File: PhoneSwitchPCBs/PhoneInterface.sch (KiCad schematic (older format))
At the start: 14 parts

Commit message: Update notes based on changing plans, minor changes to schematics and sim files
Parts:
- removed K?: Relay_DPDT, symbol PhoneInterfaceParts:Relay_DPDT
- added K?: EC2-5NU, Relay_THT:Relay_DPDT_Kemet_EC2, symbol Relay:EC2-5NU
- C? (x2): value 3.9u -> 3.3u
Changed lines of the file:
@@
 P 5250 2850
 F 0 "C?" H 5158 2804 50  0000 R CNN
-F 1 "3.9u" H 5158 2895 50  0000 R CNN
+F 1 "3.3u" H 5158 2895 50  0000 R CNN
 F 2 "" H 5250 2850 50  0001 C CNN
 F 3 "~" H 5250 2850 50  0001 C CNN
@@
 P 5250 4350
 F 0 "C?" H 5158 4304 50  0000 R CNN
-F 1 "3.9u" H 5158 4395 50  0000 R CNN
+F 1 "3.3u" H 5158 4395 50  0000 R CNN
 F 2 "" H 5250 4350 50  0001 C CNN
 F 3 "~" H 5250 4350 50  0001 C CNN
@@
 Wire Wire Line
 	5700 3650 5700 3800
-$Comp
-L PhoneInterfaceParts:Relay_DPDT K?
-U 1 1 60F6CD2F
-P 4400 3800
-F 0 "K?" V 5167 3800 50  0000 C CNN
-F 1 "Relay_DPDT" V 5076 3800 50  0000 C CNN
-F 2 "" H 4400 3800 50  0001 C CNN
-F 3 "" H 4400 3800 50  0001 C CNN
-	1    4400 3800
-	0    -1   -1   0
-$EndComp
 Wire Wire Line
 	5700 3650 4900 3650
@@
 Text Label 5450 3650 0    50   ~ 0
 RING
+$Comp
+L Relay:EC2-5NU K?
+U 1 1 60F657D7
+P 4400 3800
+F 0 "K?" V 5167 3800 50  0000 C CNN
+F 1 "EC2-5NU" V 5076 3800 50  0000 C CNN
+F 2 "Relay_THT:Relay_DPDT_Kemet_EC2" H 4400 3800 50  0001 C CNN
+F 3 "https://content.kemet.com/datasheets/KEM_R7002_EC2_EE2.pdf" H 4400 3800 50  0001 C CNN
+	1    4400 3800
+	0    -1   -1   0
+$EndComp
 $EndSCHEMATC

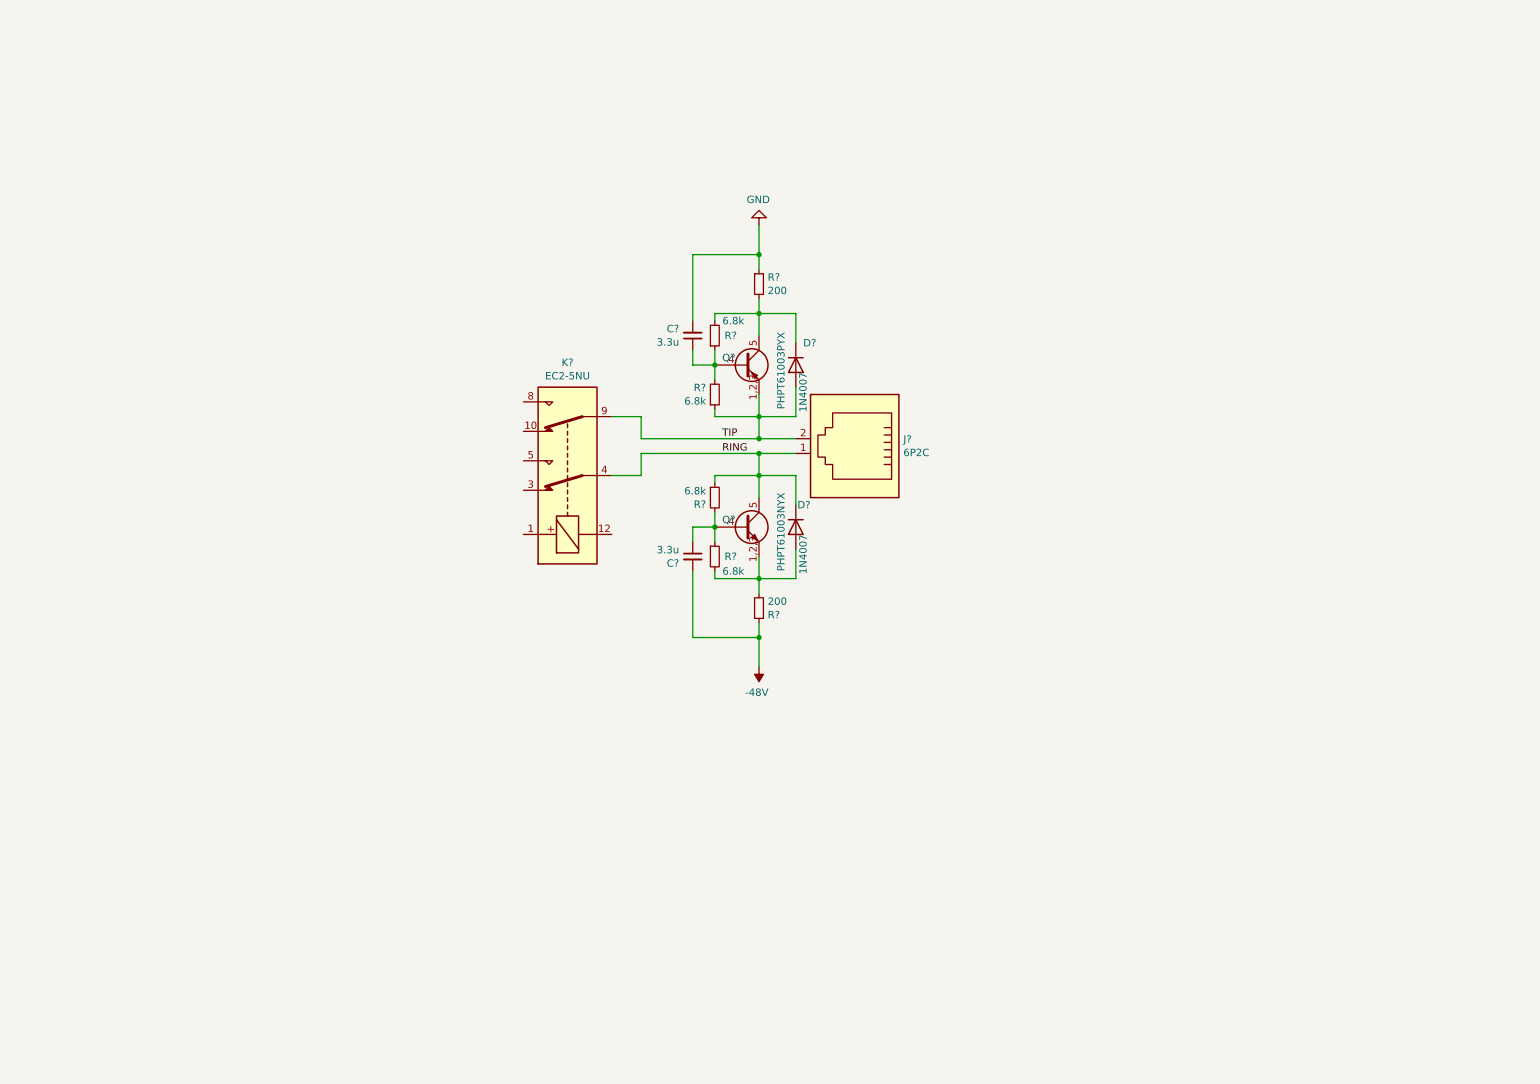
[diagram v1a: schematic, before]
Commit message: Updated schematics and notes
Changed pin count for using analog switch bypass of ring cut filter, worked more on schematics, including deciding to put routing on line modules.
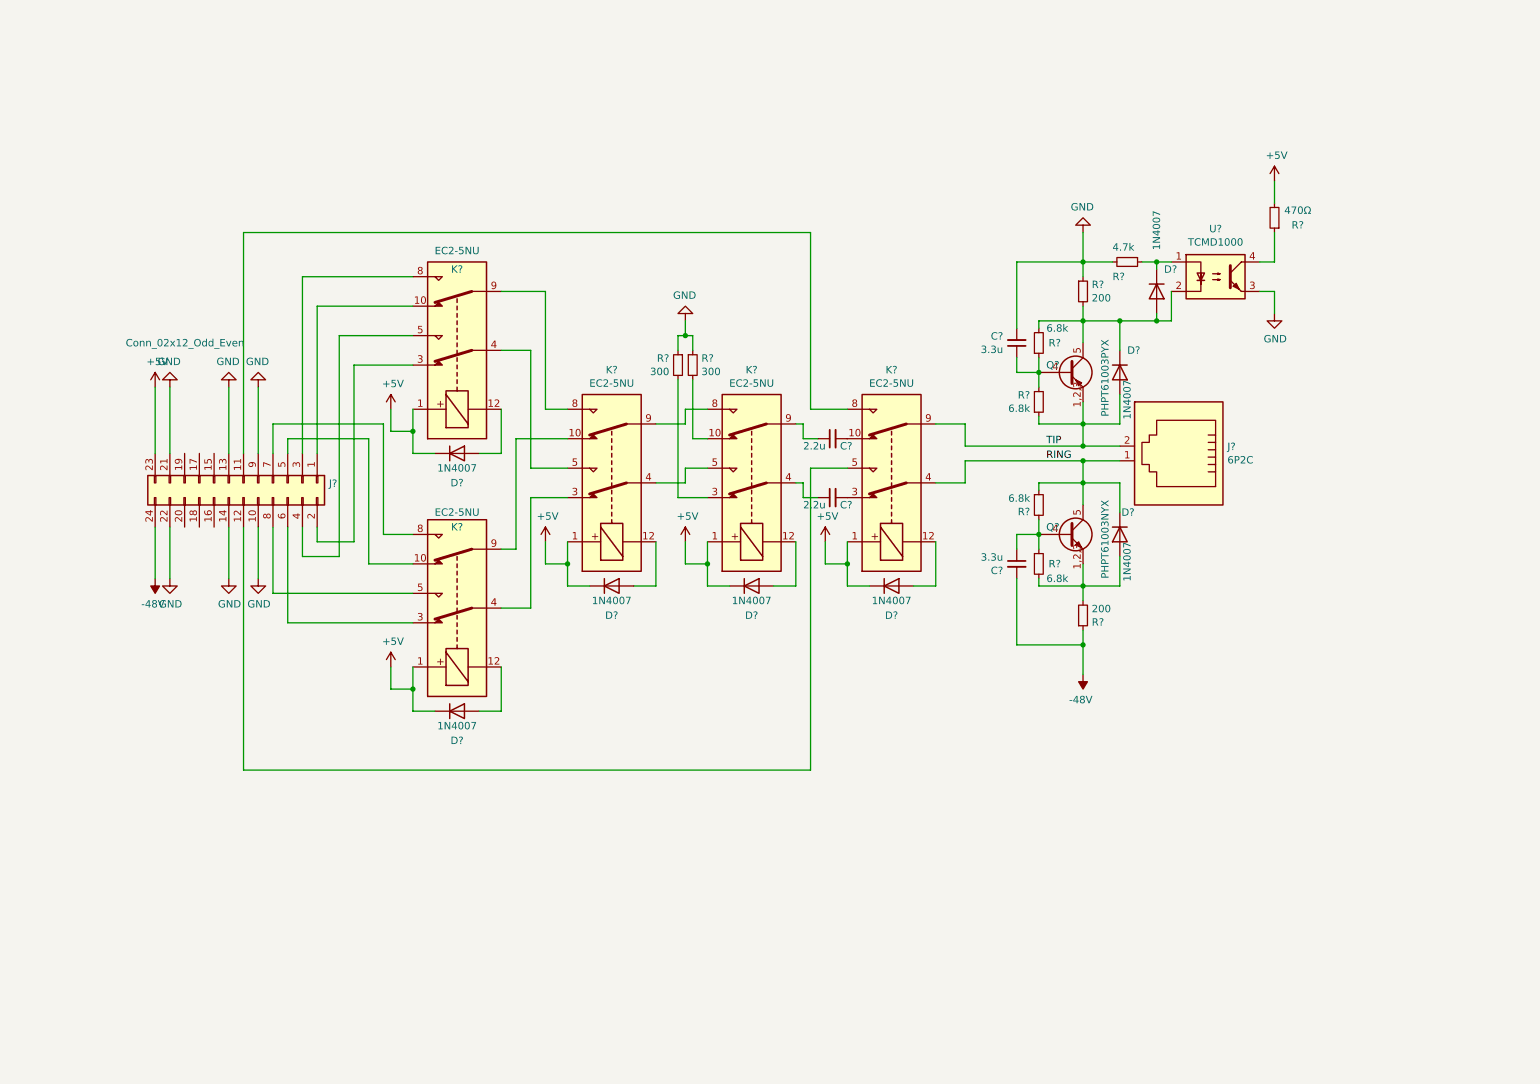
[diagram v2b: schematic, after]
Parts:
- added C? (x2): 2.2u, symbol Device:C_Small
- added D? (x6): 1N4007, Diode_THT:D_DO-41_SOD81_P10.16mm_Horizontal, symbol Diode:1N4007
- added J?: Conn_02x12_Odd_Even, symbol Connector_Generic:Conn_02x12_Odd_Even
- added K? (x4): EC2-5NU, Relay_THT:Relay_DPDT_Kemet_EC2, symbol Relay:EC2-5NU
- added R?: 4.7k, symbol Device:R_Small
- added R?: 470Ω, symbol Device:R_Small
- added R? (x2): 300, symbol Device:R_Small
- added U?: TCMD1000, Package_SO:SOP-4_4.4x2.6mm_P1.27mm, symbol PhoneInterfaceParts:TCMD1000
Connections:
- net -48V: now also J?.24 (Pin_24)
- net GND: now also J?.10 (Pin_10), J?.13 (Pin_13), J?.14 (Pin_14), J?.21 (Pin_21), J?.22 (Pin_22), J?.9 (Pin_9), R?.1, R?.1, R?.2, U?.3
- net at D?.1 (K), Q?.5 (C), R?.2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: now also D?.2 (A), U?.2
- net +5V: now reaches K?.1
- net +5V: now also D?.1 (K), D?.1 (K), D?.1 (K), D?.1 (K), D?.1 (K), J?.23 (Pin_23), K?.1, K?.1, K?.1, K?.1, R?.2
- net at K?.10: now also C?.2
- net at K?.12: now also D?.2 (A)
- net at K?.3: now also C?.2
- net at K?.5: now also J?.12 (Pin_12)
- net at K?.8: now also J?.11 (Pin_11)
- new net: D?.1 (K), R?.1, U?.1
- new net: R?.1, U?.4
- new net: K?.10, R?.2
- new net: D?.2 (A), K?.12 (x4)
- new net: K?.3, R?.2
- new net: C?.1, K?.4
- new net: K?.4, K?.5 (x2)
- new net: K?.8, K?.9 (x2)
- new net: C?.1, K?.9
- new net: K?.10, K?.9
- new net: K?.3, K?.4
- new net: J?.1 (Pin_1), K?.10
- new net: J?.2 (Pin_2), K?.3
- new net: J?.4 (Pin_4), K?.5
- new net: J?.3 (Pin_3), K?.8
- new net: J?.5 (Pin_5), K?.10
- new net: J?.6 (Pin_6), K?.3
- new net: J?.8 (Pin_8), K?.5
- new net: J?.7 (Pin_7), K?.8
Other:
- moved on the sheet: C?, D?, J?, K?, Q?, R?

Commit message: Update notes and progress on schematics
Further work on station card schematics, changed some things in notes.
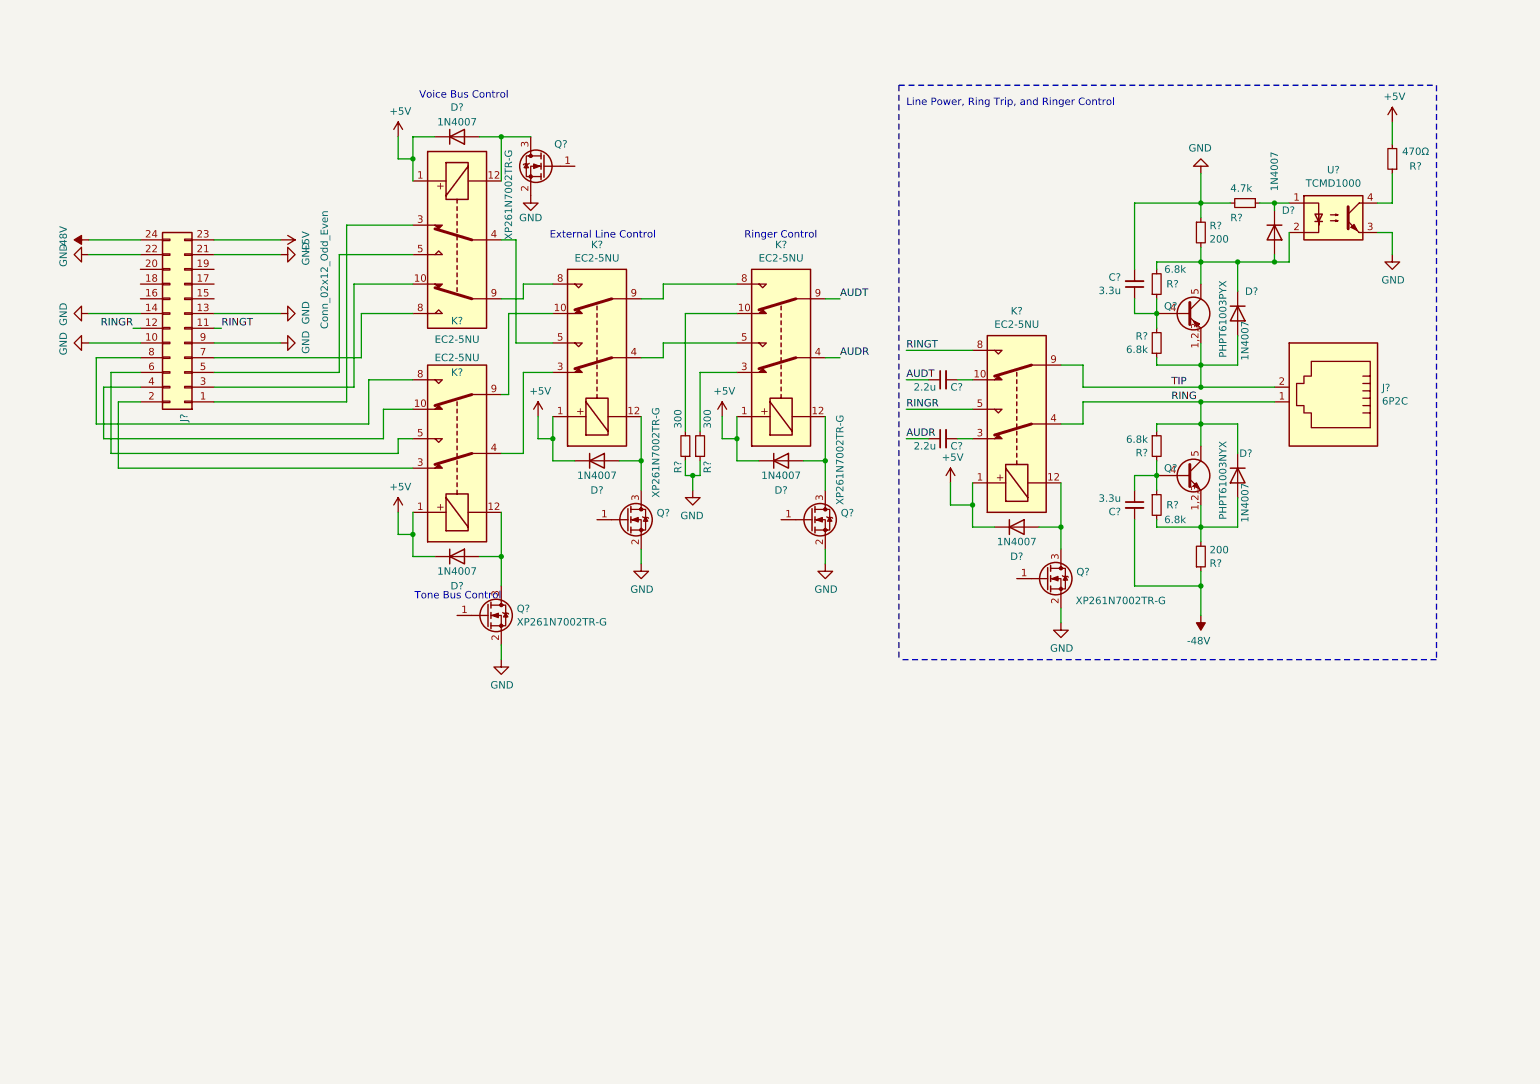
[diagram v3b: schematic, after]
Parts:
- added Q? (x5): XP261N7002TR-G, Package_TO_SOT_SMD:SOT-23, symbol PhoneInterfaceParts:XP261N7002TR-G
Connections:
- net GND: now also Q?.2 (S), Q?.2 (S), Q?.2 (S), Q?.2 (S), Q?.2 (S)
- net at D?.2 (A), K?.12: now also Q?.3 (D) (x5)
- net RINGR: now reaches J?.12 (Pin_12), K?.5
- net RINGT: now reaches J?.11 (Pin_11), K?.8
- net at K?.10: now also R?.2; no longer R?.2
- net at K?.3: now also R?.2; no longer R?.2
- net AUDR: now reaches C?.1, K?.4
- net AUDT: now reaches C?.1, K?.9
- net at K?.10: now also J?.3 (Pin_3); no longer J?.1 (Pin_1)
- net at K?.3: now also J?.1 (Pin_1); no longer J?.2 (Pin_2)
- net at K?.5: now also J?.5 (Pin_5); no longer J?.4 (Pin_4)
- net at K?.8: now also J?.7 (Pin_7); no longer J?.3 (Pin_3)
- net at K?.10: now also J?.4 (Pin_4); no longer J?.5 (Pin_5)
- net at K?.3: now also J?.2 (Pin_2); no longer J?.6 (Pin_6)
- net at K?.5: now also J?.6 (Pin_6); no longer J?.8 (Pin_8)
- net at K?.8: now also J?.8 (Pin_8); no longer J?.7 (Pin_7)
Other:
- note added: "External Line Control"
- note added: "Line Power, Ring Trip, and Ringer Control"
- note added: "Ringer Control"
- note added: "Tone Bus Control"
- note added: "Voice Bus Control"
- moved on the sheet: C?, D?, J?, K?, Q?, R?, U?

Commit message: Continued work on schematic
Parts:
- added C?: 1u, symbol Device:C_Small
- added R? (x5): 1k, symbol Device:R_Small
- added R? (x5): 100Ω, symbol Device:R_Small
- added R? (x2): 47k, symbol Device:R_Small
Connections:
- net GND: now also C?.2, R?.1, R?.1, R?.1, R?.1, R?.2; no longer J?.21 (Pin_21)
- net at R?.1, U?.4: now also R?.1
- net at Q?.1 (G): now also R?.2, R?.2 (x3)
- net at Q?.1 (G): now also R?.1, R?.1
- net AUDE: now reaches J?.15 (Pin_15)
- net AUDE: now also R?.1
- net RINGE: now reaches J?.16 (Pin_16)
- net RINGE: now also R?.1
- net TONE: now reaches J?.17 (Pin_17)
- net TONE: now also R?.2
- net LINE: now reaches J?.18 (Pin_18)
- net LINE: now also R?.1
- net VOICE: now reaches J?.20 (Pin_20)
- net VOICE: now also R?.2
- net at Q?.1 (G): now also R?.1, R?.2
- new net: C?.1, R?.1, R?.2
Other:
- note added: "Audio Enable Control"
- moved on the sheet: C?, D?, J?, K?, Q?, R?, U?

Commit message: Continue work on schematic and add more notes
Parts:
- added C?: 1u, symbol Device:C_Small
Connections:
- net GND: now also C?.1
- net HOOKS: now reaches R?.1, R?.1, U?.4
- net at R?.2: now also C?.2
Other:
- moved on the sheet: C?, R?
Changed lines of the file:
@@
 L Device:R_Small R?
 U 1 1 618AB787
-P 9600 1500
-F 0 "R?" H 9400 1550 50  0000 L CNN
-F 1 "47k" H 9350 1450 50  0000 L CNN
-F 2 "" H 9600 1500 50  0001 C CNN
-F 3 "~" H 9600 1500 50  0001 C CNN
-	1    9600 1500
+P 8850 3400
+F 0 "R?" V 8950 3400 50  0000 L CNN
+F 1 "47k" V 8950 3250 50  0000 L CNN
+F 2 "" H 8850 3400 50  0001 C CNN
+F 3 "~" H 8850 3400 50  0001 C CNN
+	1    8850 3400
 	0    -1   -1   0
 $EndComp
@@
 L Device:C_Small C?
 U 1 1 618ABAFE
-P 9800 1700
-F 0 "C?" H 9708 1654 50  0000 R CNN
-F 1 "1u" H 9708 1745 50  0000 R CNN
-F 2 "" H 9800 1700 50  0001 C CNN
-F 3 "~" H 9800 1700 50  0001 C CNN
-	1    9800 1700
+P 9100 3600
+F 0 "C?" H 9008 3554 50  0000 R CNN
+F 1 "1u" H 9008 3645 50  0000 R CNN
+F 2 "" H 9100 3600 50  0001 C CNN
+F 3 "~" H 9100 3600 50  0001 C CNN
+	1    9100 3600
 	-1   0    0    -1
 $EndComp
-Wire Wire Line
-	9800 1600 9800 1500
-Wire Wire Line
-	9800 1500 9700 1500
-Wire Wire Line
-	9500 1500 9400 1500
-Connection ~ 9400 1500
 $Comp
 L power:GND #PWR?
 U 1 1 618BB6CA
-P 9800 1850
-F 0 "#PWR?" H 9800 1600 50  0001 C CNN
-F 1 "GND" H 9805 1677 50  0000 C CNN
-F 2 "" H 9800 1850 50  0001 C CNN
-F 3 "" H 9800 1850 50  0001 C CNN
-	1    9800 1850
+P 9100 3850
+F 0 "#PWR?" H 9100 3600 50  0001 C CNN
+F 1 "GND" H 9105 3677 50  0000 C CNN
+F 2 "" H 9100 3850 50  0001 C CNN
+F 3 "" H 9100 3850 50  0001 C CNN
+	1    9100 3850
+	1    0    0    -1
+$EndComp
+$Comp
+L Device:R_Small R?
+U 1 1 618CAA0B
+P 9400 3400
+F 0 "R?" V 9500 3400 50  0000 L CNN
+F 1 "47k" V 9500 3250 50  0000 L CNN
+F 2 "" H 9400 3400 50  0001 C CNN
+F 3 "~" H 9400 3400 50  0001 C CNN
+	1    9400 3400
+	0    -1   -1   0
+$EndComp
+$Comp
+L Device:C_Small C?
+U 1 1 61907E2B
+P 9700 3600
+F 0 "C?" H 9608 3554 50  0000 R CNN
+F 1 "1u" H 9608 3645 50  0000 R CNN
+F 2 "" H 9700 3600 50  0001 C CNN
+F 3 "~" H 9700 3600 50  0001 C CNN
+	1    9700 3600
+	1    0    0    1
+$EndComp
+Wire Wire Line
+	9400 1500 9450 1500
+Connection ~ 9400 1500
+Text Label 9450 1500 0    50   ~ 0
+HOOKS
+Text Label 8700 3400 2    50   ~ 0
+HOOKS
+Wire Wire Line
+	9100 3500 9100 3400
+Wire Wire Line
+	9100 3400 8950 3400
+Wire Wire Line
+	9100 3850 9100 3700
+Wire Wire Line
+	9300 3400 9100 3400
+Connection ~ 9100 3400
+Wire Wire Line
+	9700 3500 9700 3400
+Wire Wire Line
+	9700 3400 9500 3400
+$Comp
+L power:GND #PWR?
+U 1 1 619B703E
+P 9700 3850
+F 0 "#PWR?" H 9700 3600 50  0001 C CNN
+F 1 "GND" H 9705 3677 50  0000 C CNN
+F 2 "" H 9700 3850 50  0001 C CNN
+F 3 "" H 9700 3850 50  0001 C CNN
+	1    9700 3850
 	1    0    0    -1
 $EndComp
 Wire Wire Line
-	9800 1800 9800 1850
-$Comp
-L Device:R_Small R?
-U 1 1 618CAA0B
-P 10050 1500
-F 0 "R?" H 9850 1550 50  0000 L CNN
-F 1 "47k" H 9800 1450 50  0000 L CNN
-F 2 "" H 10050 1500 50  0001 C CNN
-F 3 "~" H 10050 1500 50  0001 C CNN
-	1    10050 1500
-	0    -1   -1   0
-$EndComp
+	9700 3850 9700 3700
 Wire Wire Line
-	9950 1500 9800 1500
-Connection ~ 9800 1500
+	8700 3400 8750 3400
 $EndSCHEMATC
